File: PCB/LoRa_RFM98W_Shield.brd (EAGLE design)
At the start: 53.6 x 59.9 mm, 40 parts, among them IC1 SHT20, IC2 TXS0102DCUR, J1 TYPE-C-31-M-17, J2 CON_TERMINAL_BLOCK_03-5MM, U1 XC6206P332MR, U2 RFM98W, X1 BU-SMA-H

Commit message: cleanup & PCB minor update
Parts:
- removed C4: 100nF, rcl:C0603
- removed R3: 10k, rcl:R0603
- C1, C3, C5, C6, C7, C9: device rcl:C0603 -> angrypig7-RCL:C0603
- C2: device rcl:C0805 -> angrypig7-RCL:C0805
- D1: device dp_devices:SOD-123 -> angrypig7-Diodes:SOD-123
- J1: value TYPE-C-31-M-17 -> USB-TYPE-C-31-M-17; device angrypig7_Library:TYPE-C-31-M-17 -> angrypig7-Connectors:TYPE-C-31-M-17
- J2: value CON_TERMINAL_BLOCK_03-5MM -> CON_TERMINAL_BLOCK_02-5MM; device dp_devices:TERMINAL_BLOCK_3P_5 -> dp_devices:TERMINAL_BLOCK_2P_5
- R1, R10, R11, R12, R2, R4, R5, R6, R7, R8, R9: device rcl:R0603 -> angrypig7-RCL:R0603
- moved C1 2.09 mm to (44.7, 17.5)
- moved D1 2.09 mm to (44.7, 15.2)
- moved J2 1.44 mm to (17.8, 9.40)
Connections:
- net GND: now also J2.1; no longer C4.1, J2.2, R3.1
- net INPUT_RELAY_STATUS: no longer C4.2, J2.1, R3.2
- net N$8: now also J2.2; no longer J2.3
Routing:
- net INPUT_RELAY_STATUS: track 15.9 -> 2.90 mm
- net N$1: track 11.9 -> 9.63 mm
- net N$16: track 20.5 -> 18.7 mm
- net I2C_SCL_5V: track 65.4 -> 66.9 mm
- net GND: vias 42 -> 43
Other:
- board text added: ">CNAME"
- board text removed: "LoRa Shield"

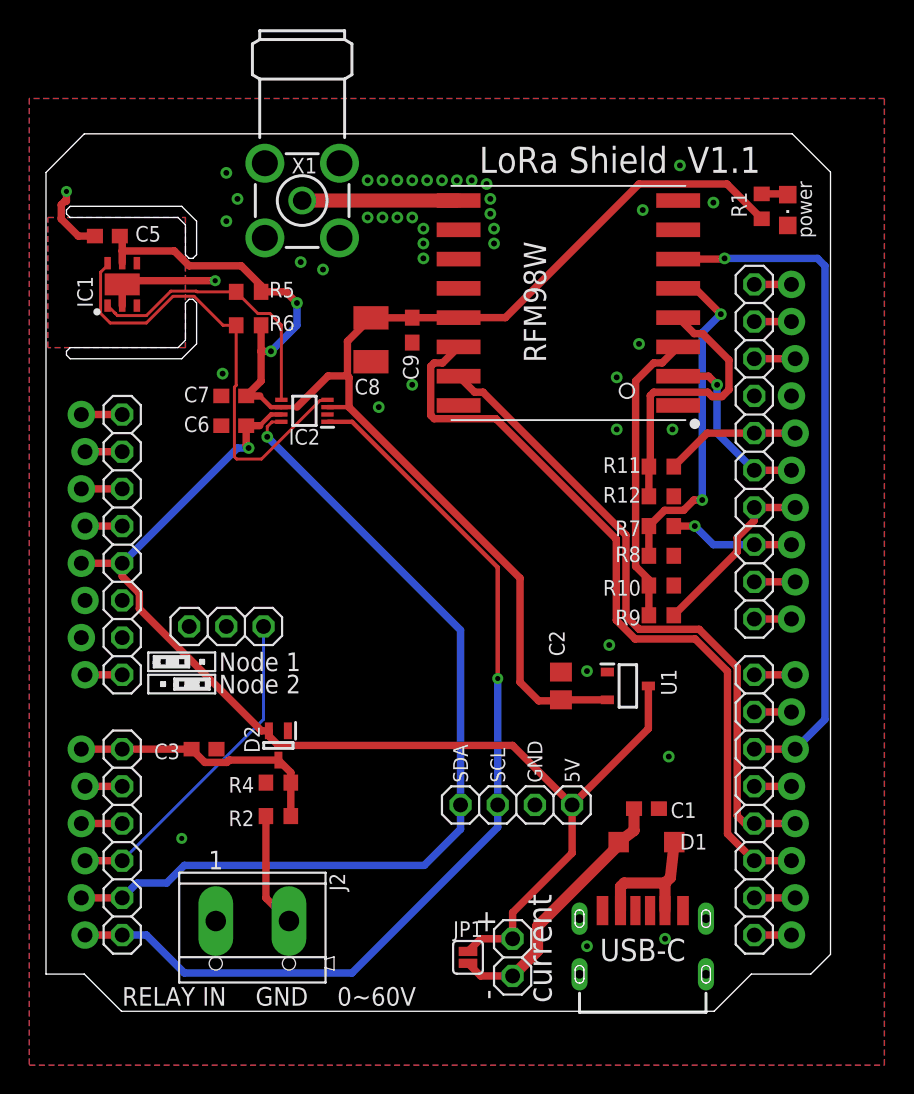
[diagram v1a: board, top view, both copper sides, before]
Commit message: PCB minor update
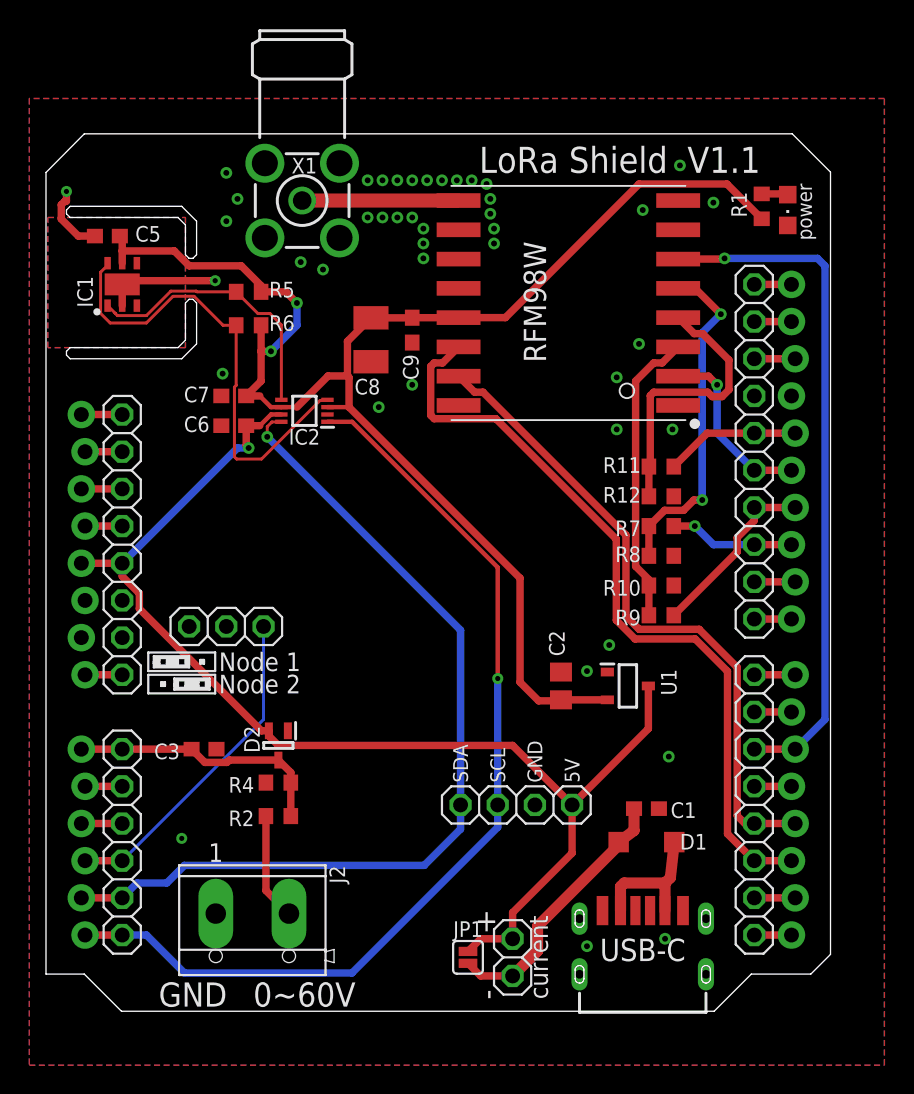
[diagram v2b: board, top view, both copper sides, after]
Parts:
- moved J2 0.51 mm to (17.8, 9.91)
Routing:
- net N$8: track 7.82 -> 7.31 mm
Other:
- board text removed: "RELAY IN"
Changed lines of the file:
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@@
 <text x="35.052" y="19.304" size="1.016" layer="21" ratio="12" rot="R90">SCL</text>
 <text x="32.512" y="19.304" size="1.016" layer="21" ratio="12" rot="R90">SDA</text>
-<text x="36.576" y="11.684" size="1.651" layer="21" ratio="12" rot="R90" align="top-right">current</text>
+<text x="37.338" y="7.366" size="1.27" layer="21" font="vector" ratio="12" rot="R90" align="center">current</text>
 <wire x1="10.668" y1="28.194" x2="15.24" y2="28.194" width="0.1524" layer="21"/>
 <wire x1="15.24" y1="28.194" x2="15.24" y2="26.924" width="0.1524" layer="21"/>
@@
 <wire x1="14.859" y1="26.162" x2="14.859" y2="26.035" width="0.1524" layer="21"/>
 <wire x1="14.859" y1="26.035" x2="14.732" y2="26.035" width="0.1524" layer="21"/>
-<text x="15.494" y="26.924" size="1.27" layer="21" ratio="15" rot="R180" align="top-right">Node 1</text>
-<text x="15.494" y="25.4" size="1.27" layer="21" ratio="15" rot="R180" align="top-right">Node 2</text>
-<text x="16.002" y="5.334" size="1.27" layer="21" ratio="12" rot="R180">RELAY IN</text>
-<text x="21.59" y="5.334" size="1.27" layer="21" ratio="12" rot="R180">GND</text>
-<text x="28.956" y="5.334" size="1.27" layer="21" ratio="12" rot="R180">0~60V</text>
+<text x="15.494" y="26.924" size="1.27" layer="21" font="vector" ratio="15" rot="R180" align="top-right">Node 1</text>
+<text x="15.494" y="25.4" size="1.27" layer="21" font="vector" ratio="15" rot="R180" align="top-right">Node 2</text>
+<text x="13.716" y="4.826" size="1.651" layer="21" font="vector" ratio="15" rot="R180" align="center">GND</text>
+<text x="21.336" y="4.826" size="1.651" layer="21" font="vector" ratio="15" rot="R180" align="center">0~60V</text>
 <text x="33.782" y="9.906" size="1.524" layer="21" ratio="12" align="center">+</text>
 <text x="33.782" y="4.826" size="1.524" layer="21" ratio="12" rot="R90" align="center">-</text>
 <wire x1="14.224" y1="27.559" x2="14.478" y2="27.559" width="0.1524" layer="21"/>
 <wire x1="11.557" y1="26.035" x2="11.811" y2="26.035" width="0.1524" layer="21"/>
-<text x="54.991" y="56.515" size="1.016" layer="21" ratio="12" rot="R90" align="top-left">power</text>
-<text x="33.274" y="62.738" size="1.778" layer="21" ratio="15" align="top-left">&gt;CNAME</text>
-<text x="36.322" y="48.006" size="1.524" layer="21" ratio="12" rot="R90" align="top-left">RFM98W</text>
-<text x="47.498" y="62.738" size="1.778" layer="21" ratio="15" align="top-left">&gt;CREVISION</text>
+<text x="55.499" y="58.293" size="1.016" layer="21" font="vector" ratio="12" rot="R90" align="center">power</text>
+<text x="33.274" y="62.738" size="1.778" layer="21" font="vector" ratio="15" align="top-left">&gt;CNAME</text>
+<text x="36.322" y="48.006" size="1.524" layer="21" font="vector" ratio="12" rot="R90" align="top-left">RFM98W</text>
+<text x="47.498" y="62.738" size="1.778" layer="21" font="vector" ratio="15" align="top-left">&gt;CREVISION</text>
 </plain>
 <attributes>
@@
 <attribute name="VALUE" x="4.826" y="52.832" size="1.0668" layer="27" font="vector" ratio="15" rot="R90" align="center"/>
 </element>
-<element name="J2" library="dp_devices" package="TERMINAL_BLOCK_2P_5" value="CON_TERMINAL_BLOCK_02-5MM" x="17.78" y="9.398" smashed="yes" rot="R180">
-<attribute name="NAME" x="23.05" y="13.128" size="1.0668" layer="25" font="vector" ratio="15" rot="R270"/>
+<element name="J2" library="dp_devices" package="TERMINAL_BLOCK_2P_5" value="CON_TERMINAL_BLOCK_02-5MM" x="17.78" y="9.906" smashed="yes" rot="R180">
+<attribute name="NAME" x="23.05" y="13.636" size="1.0668" layer="25" font="vector" ratio="15" rot="R270"/>
 </element>
 </elements>
@@
 <contactref element="R2" pad="2"/>
 <contactref element="J2" pad="2"/>
-<wire x1="20.28" y1="9.848" x2="18.708" y2="11.42" width="0.508" layer="1"/>
-<wire x1="18.708" y1="11.42" x2="18.708" y2="17.018" width="0.508" layer="1"/>
+<wire x1="20.279996875" y1="10.356003125" x2="18.708003125" y2="11.927996875" width="0.508" layer="1"/>
+<wire x1="18.708003125" y1="11.927996875" x2="18.708" y2="17.018" width="0.508" layer="1"/>
+<wire x1="20.279996875" y1="10.356003125" x2="20.28" y2="10.356" width="0" layer="19" extent="1-1"/>
 </signal>
 <signal name="SPI_MOSI_5V">

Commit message: library update
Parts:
- J1: device angrypig7-Connectors:TYPE-C-31-M-17 -> angrypig7-Connectors:USB-TYPE-C-31-M-17
- moved J1 0.36 mm to (44.7, 10.4)
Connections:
- net GND: now also J1.SHLD-B1, J1.SHLD-B2, J1.SHLD-B3, J1.SHLD-B4, J1.SHLD-T1, J1.SHLD-T2, J1.SHLD-T3, J1.SHLD-T4; no longer J1.P$1, J1.P$2, J1.P$3, J1.P$4
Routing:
- net N$1: track 9.63 -> 10.3 mm
- net GND: vias 43 -> 42
